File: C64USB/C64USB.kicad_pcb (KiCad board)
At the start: 2 copper layers, 33.8 x 64.2 mm, 31 parts, among them J1 Keyboard, J2 USB_B_Micro, J3 AVR-ISP-6, J4 Joystick1, J5 Joystick2, J6 LED, U2 ATmega88-20A, Y1 16MHz

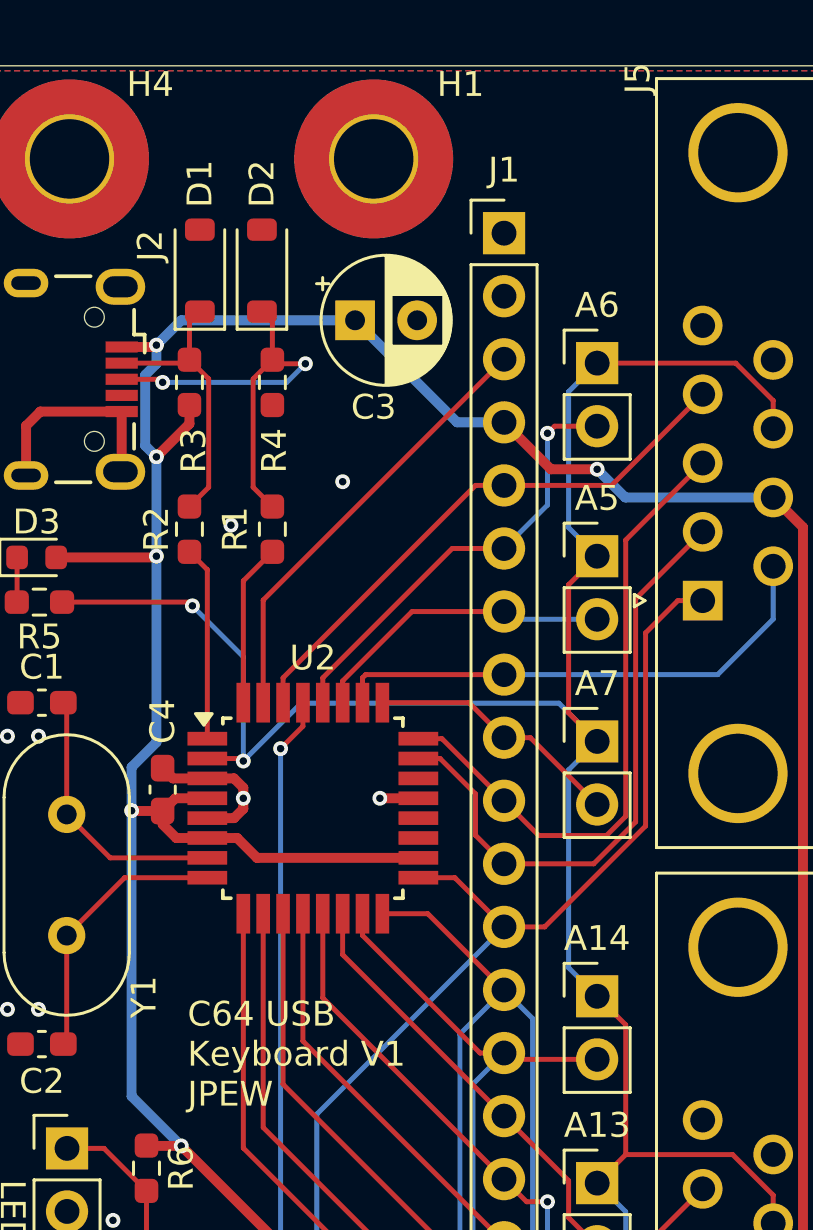
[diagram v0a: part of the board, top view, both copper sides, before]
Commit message: Clamp D- pull up voltage
Clamps the D- pull up to ~3.3V using the simple technique of two
1N4148 diodes. Some USB host controllers are sensitive to the D- line
being pulled up to 5V (even with the 1.5K pull up resistor) and will
refuse to enumerate the device if it does so. For some reason, the TVS
diodes are not clamping the output to 3.6V.

This was particularly noticed when using the board with a Raspberry Pi
4.
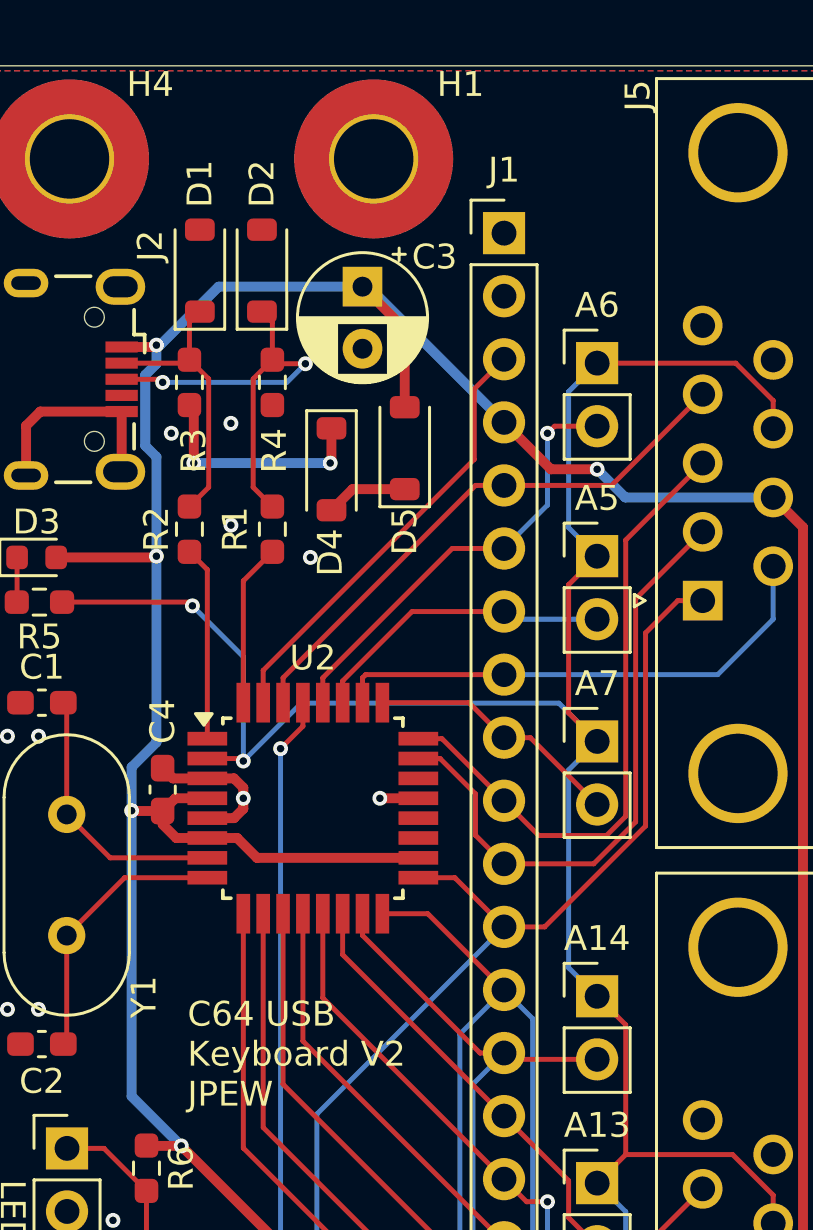
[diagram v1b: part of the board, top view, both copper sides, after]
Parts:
- added D4: 1N4148, Diode_SMD:D_SOD-123, F.Cu at (132.1, 69.2)
- added D5: 1N4148, Diode_SMD:D_SOD-123, F.Cu at (135.0, 68.4)
- moved C3 1.39 mm to (133.3, 61.9), turned to -90 degrees
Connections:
- R3 pad 2: /PWR -> Net-(D4-K)
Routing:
- net Net-(D4-K): track 0.00 -> 9.33 mm, vias 0 -> 2
- net /PWR: track 140.9 -> 144.9 mm, vias 6 -> 5
- net Net-(D4-A): track 0.00 -> 3.30 mm
- net GNDREF: vias 10 -> 12
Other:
- board text added: "C64 USB Keyboard V2 JPEW"
- board text removed: "C64 USB Keyboard V1 JPEW"

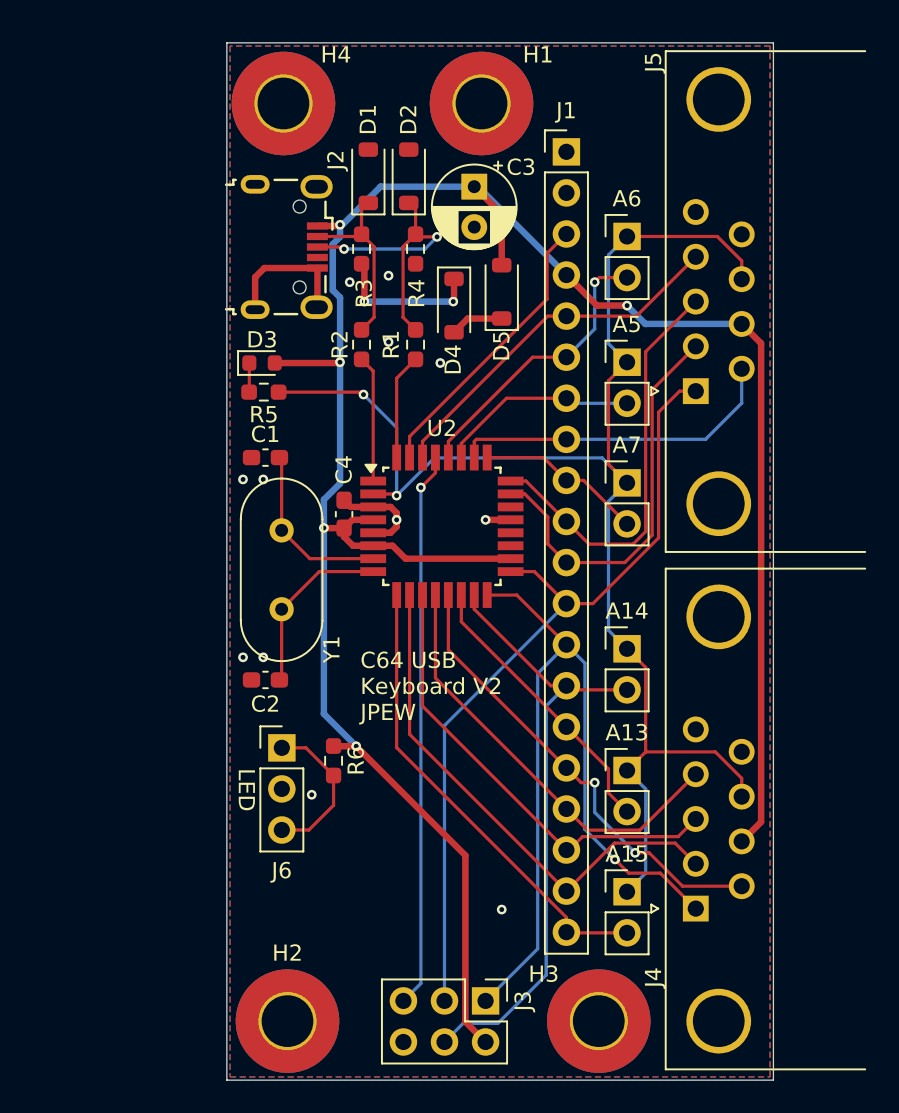
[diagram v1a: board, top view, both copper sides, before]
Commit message: Replace micro-USB connector with USB-B
The micro USB connector is very difficult to solder correctly, so
replace it with a USB-B connector which should be much easier
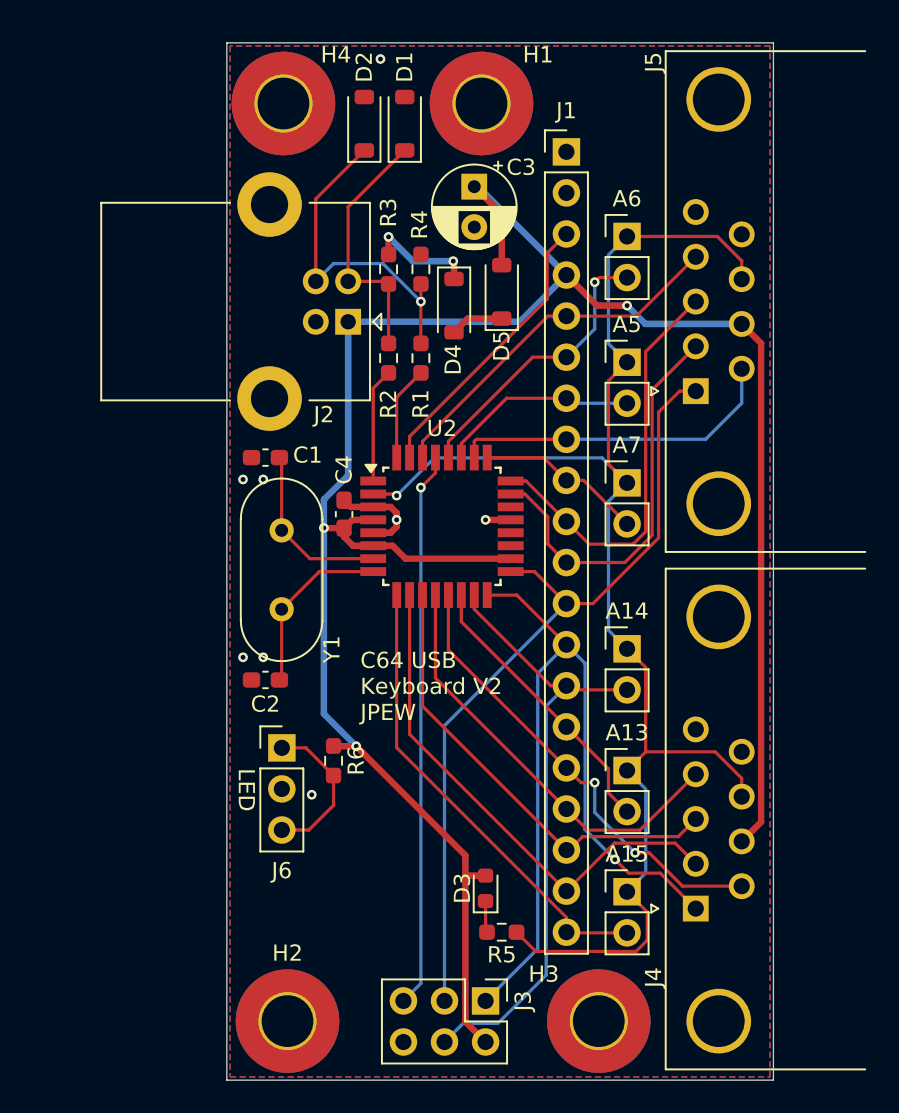
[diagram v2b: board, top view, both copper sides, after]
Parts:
- J2: value USB_B_Micro -> USB_B; footprint Connector_USB:USB_Micro-B_Wuerth_629105150521 -> Connector_USB:USB_B_Lumberg_2411_02_Horizontal
- moved R5 36.5 mm to (135.0, 108.0)
- moved D3 35.3 mm to (134.0, 105.3), turned to 90 degrees
- moved J2 5.99 mm to (125.5, 70.2), turned to 180 degrees
- moved D2 4.26 mm to (126.5, 58.0)
- moved D1 3.95 mm to (129.0, 58.0)
- moved R3 2.09 mm to (128.0, 67.0), turned to 90 degrees
- moved R2 1.87 mm to (128.0, 72.5)
- moved R4 1.29 mm to (130.0, 67.0), turned to -90 degrees
- moved R1 0.90 mm to (130.0, 72.5)
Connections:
- J2 pad 4: unconnected-(J2-ID-Pad4) -> GNDREF
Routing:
- net GNDREF: track 16.1 -> 7.58 mm, vias 12 -> 8
- net /PWR: track 144.9 -> 139.9 mm, vias 5 -> 3
- net /D-: track 11.5 -> 15.8 mm
- net /D+: track 17.8 -> 20.9 mm, vias 2 -> 1
- net Net-(D4-K): track 9.33 -> 6.83 mm
- net Net-(U2-PD3): track 7.82 -> 7.08 mm
- net Net-(U2-PD2): track 6.56 -> 5.86 mm
- net /AUX: vias 2 -> 1

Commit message: Use custom symbol and footprint for keyboard header
This one correctly omits the key pin
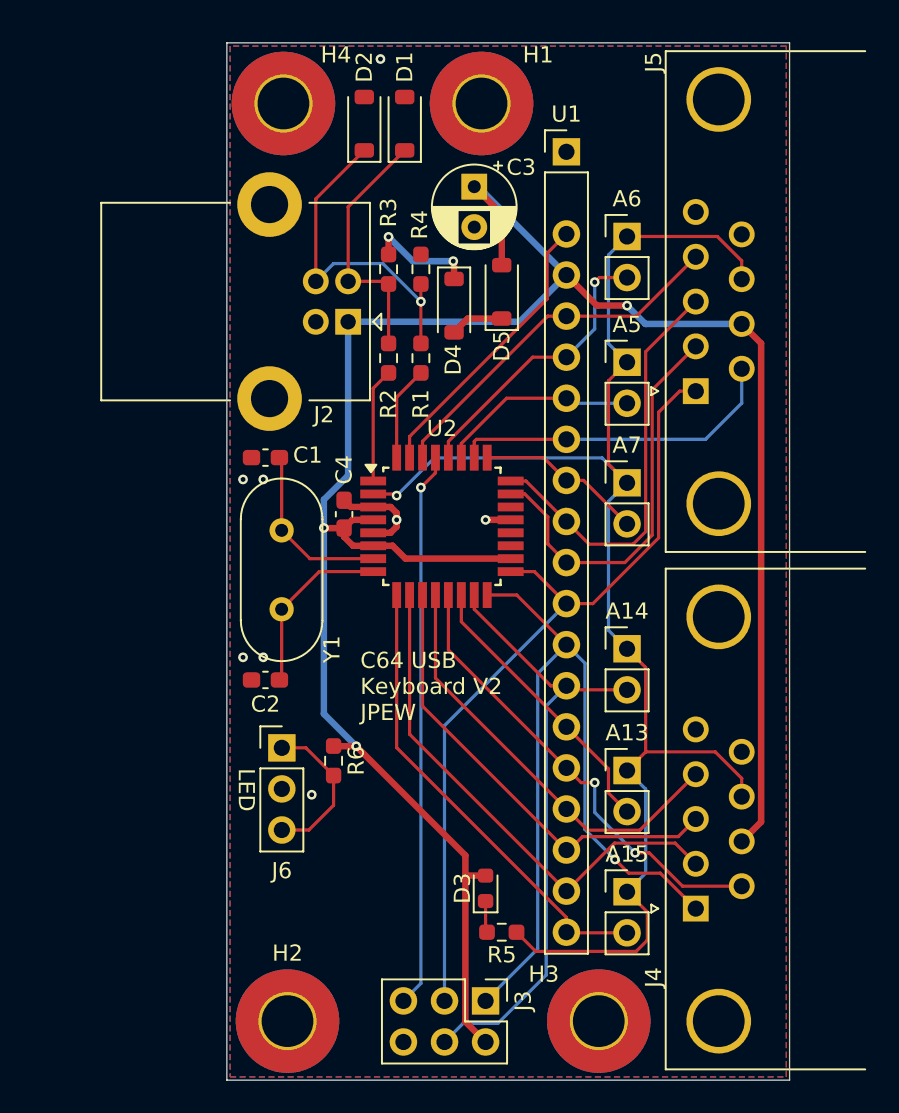
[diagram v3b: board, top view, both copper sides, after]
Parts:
- removed J1: Keyboard, Connector_PinHeader_2.54mm:PinHeader_1x20_P2.54mm_Vertical
- added U1: ~, C64:C64_Keyboard_Header, F.Cu at (139.0, 59.7)
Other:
- board size 33.8 x 64.2 mm -> 34.8 x 64.2 mm

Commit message: Allow more space for keyboard header
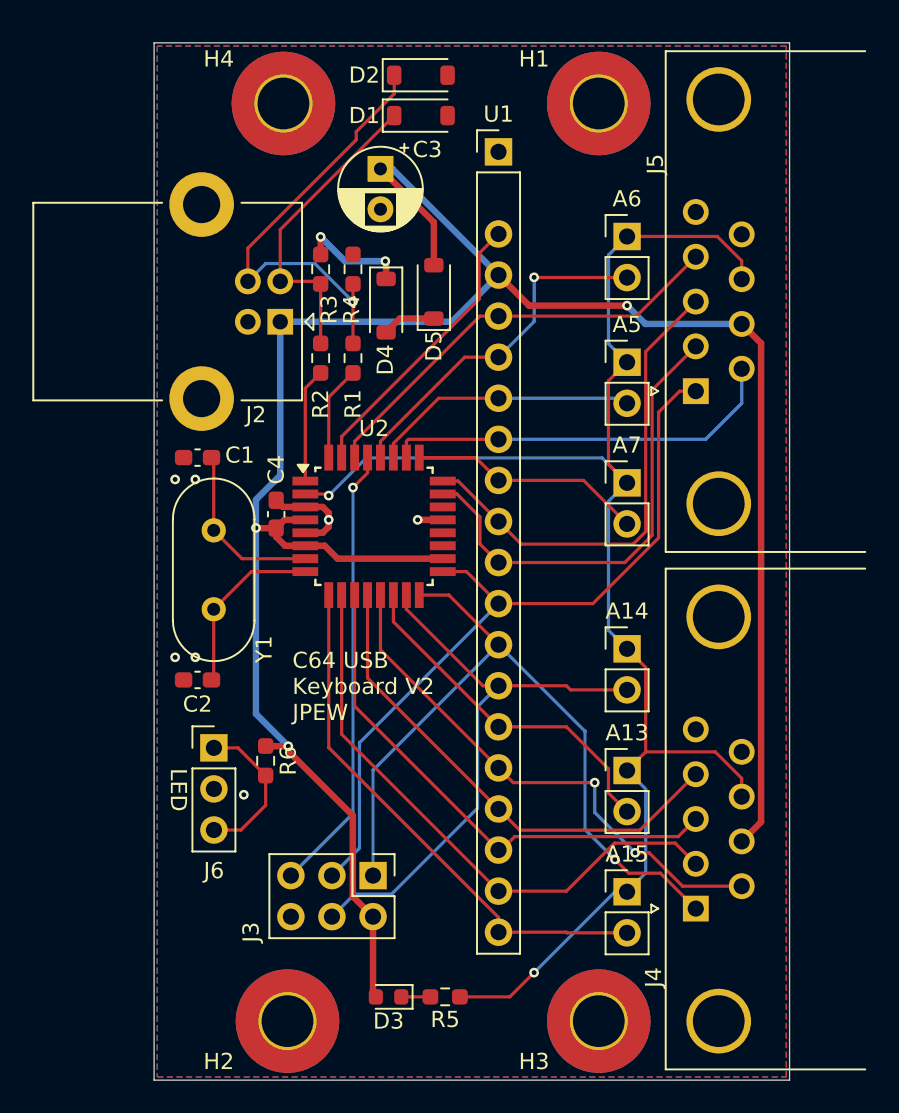
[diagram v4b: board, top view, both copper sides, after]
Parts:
- moved J3 10.4 mm to (127.0, 104.5)
- moved D3 9.00 mm to (128.0, 112.0), turned to 180 degrees
- moved H1 7.25 mm to (141.0, 56.8)
- moved C3 5.90 mm to (127.5, 60.8)
- moved R5 5.32 mm to (131.5, 112.0)
- moved D2 4.61 mm to (130.0, 55.0), turned to 0 degrees
- moved D4 4.20 mm to (127.8, 69.2)
- moved U2 4.20 mm to (127.1, 82.9)
- moved C1 4.20 mm to (116.2, 78.7)
- moved C2 4.20 mm to (116.2, 92.4)
- moved C4 4.20 mm to (121.0, 82.2)
- moved J2 4.20 mm to (121.3, 70.2)
- moved J6 4.20 mm to (117.2, 96.6)
- moved R1 4.20 mm to (125.8, 72.5)
- moved R2 4.20 mm to (123.8, 72.5)
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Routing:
- net /D+: track 20.9 -> 28.1 mm
- net /RESET: track 34.4 -> 27.8 mm
- net /ROW_0: track 51.1 -> 46.2 mm
- net /AUX: track 91.6 -> 96.5 mm, vias 1 -> 2
- net /ROW_7: track 29.0 -> 33.2 mm
- net /COL_2: track 25.8 -> 30.0 mm
- net /COL_4: track 20.7 -> 24.9 mm
- net /COL_1: track 25.0 -> 29.2 mm
- net /ROW_1: track 32.1 -> 36.3 mm
- net /ROW_3: track 26.6 -> 30.8 mm
- net /COL_5: track 12.4 -> 16.6 mm
- net /ROW_5: track 17.6 -> 21.8 mm
- net /ROW_4: track 28.7 -> 32.9 mm
- net /ROW_2: track 28.3 -> 32.5 mm
- net /COL_3: track 22.6 -> 26.8 mm
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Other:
- board size 34.8 x 64.2 mm -> 39.3 x 64.2 mm

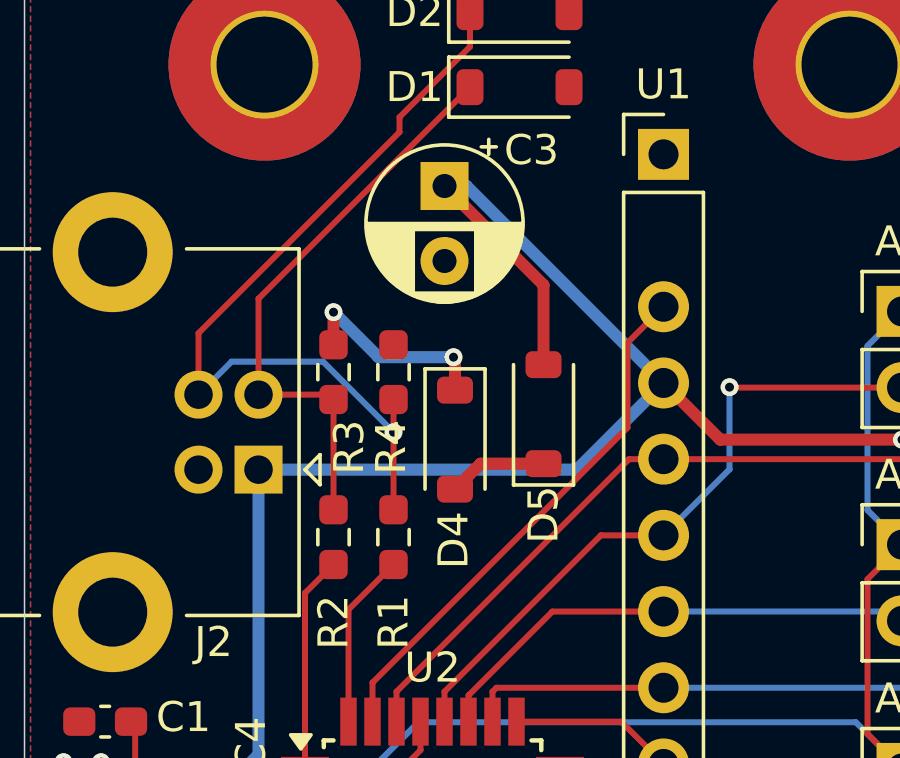
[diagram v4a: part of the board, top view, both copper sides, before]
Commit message: Remove one diode from D-
After further testing, a single diode is sufficient to allow the device
to enumerate on the problematic USB controllers. This leads me to
believe that this means the controller is actually detecting the device
being back-powered through D-, which makes a lot more sense, and the
Zener diode is sufficiently clamping the voltage
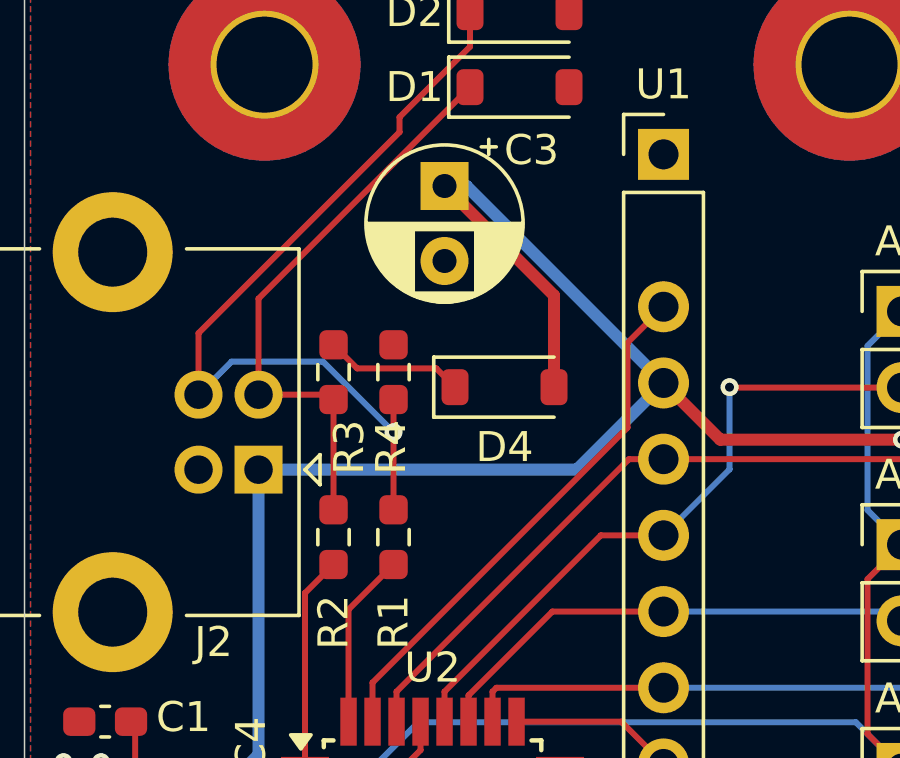
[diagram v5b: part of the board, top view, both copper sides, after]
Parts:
- removed D5: 1N4148, Diode_SMD:D_SOD-123
- moved D4 2.41 mm to (129.5, 67.5), turned to 0 degrees
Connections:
- D4 pad 2: Net-(D4-A) -> /PWR
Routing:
- net Net-(D4-A): track 3.30 -> 0.00 mm
- net Net-(D4-K): track 6.83 -> 4.64 mm, vias 2 -> 0
- net /PWR: track 142.8 -> 143.7 mm
